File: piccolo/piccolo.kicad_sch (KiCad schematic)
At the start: 18 parts, among them U1 ProMicro

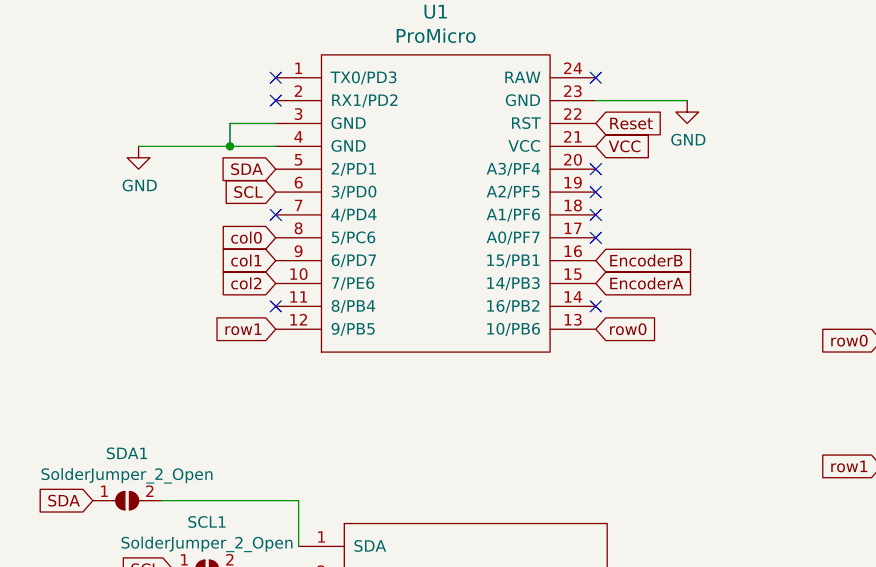
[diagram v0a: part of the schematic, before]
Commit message: flipped board, moved diodes
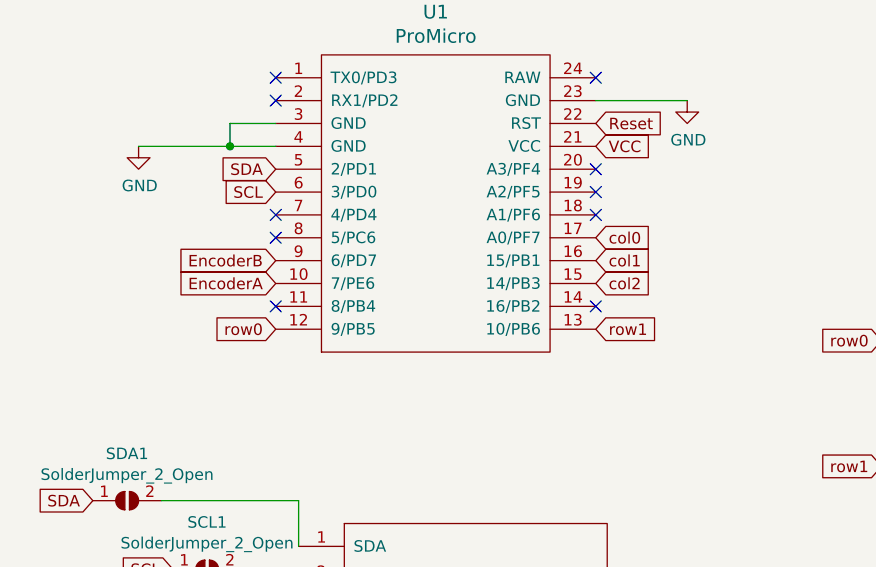
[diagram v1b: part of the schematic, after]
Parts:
- U1: footprint Envoy:ProMicro_v3 -> Envoy:ProMicro_face_in
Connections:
- net EncoderA: now also U1.10 (7/PE6); no longer U1.15 (14/PB3)
- net EncoderB: now also U1.9 (6/PD7); no longer U1.16 (15/PB1)
- net col0: now also U1.17 (A0/PF7); no longer U1.8 (5/PC6)
- net col1: now also U1.16 (15/PB1); no longer U1.9 (6/PD7)
- net col2: now also U1.15 (14/PB3); no longer U1.10 (7/PE6)
- net row0: now also U1.12 (9/PB5); no longer U1.13 (10/PB6)
- net row1: now also U1.13 (10/PB6); no longer U1.12 (9/PB5)
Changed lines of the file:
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@@
   (no_connect (at 41.91 44.45))
   (no_connect (at 41.91 57.15))
+  (no_connect (at 41.91 59.69))
   (no_connect (at 41.91 67.31))
   (no_connect (at 77.47 41.91))
@@
   (no_connect (at 77.47 54.61))
   (no_connect (at 77.47 57.15))
-  (no_connect (at 77.47 59.69))
   (no_connect (at 77.47 67.31))
   (no_connect (at 102.87 3.81))
@@
     )
   )
-  (global_label "col0" (shape input) (at 41.91 59.69 180) (fields_autoplaced)
-    (effects (font (size 1.27 1.27)) (justify right))
-    (property "Intersheet References" "${INTERSHEET_REFS}" (id 0) (at 0 0 0)
-      (effects (font (size 1.27 1.27)) hide)
-    )
-  )
-  (global_label "col1" (shape input) (at 41.91 62.23 180) (fields_autoplaced)
-    (effects (font (size 1.27 1.27)) (justify right))
-    (property "Intersheet References" "${INTERSHEET_REFS}" (id 0) (at 0 0 0)
-      (effects (font (size 1.27 1.27)) hide)
-    )
-  )
-  (global_label "col2" (shape input) (at 41.91 64.77 180) (fields_autoplaced)
-    (effects (font (size 1.27 1.27)) (justify right))
-    (property "Intersheet References" "${INTERSHEET_REFS}" (id 0) (at 0 0 0)
-      (effects (font (size 1.27 1.27)) hide)
-    )
-  )
-  (global_label "row1" (shape input) (at 41.91 69.85 180) (fields_autoplaced)
-    (effects (font (size 1.27 1.27)) (justify right))
-    (property "Intersheet References" "${INTERSHEET_REFS}" (id 0) (at 0 0 0)
+  (global_label "EncoderB" (shape input) (at 41.91 62.23 180) (fields_autoplaced)
+    (effects (font (size 1.27 1.27)) (justify right))
+    (property "Intersheet References" "${INTERSHEET_REFS}" (id 0) (at 119.38 124.46 0)
+      (effects (font (size 1.27 1.27)) hide)
+    )
+  )
+  (global_label "EncoderA" (shape input) (at 41.91 64.77 180) (fields_autoplaced)
+    (effects (font (size 1.27 1.27)) (justify right))
+    (property "Intersheet References" "${INTERSHEET_REFS}" (id 0) (at 119.38 129.54 0)
+      (effects (font (size 1.27 1.27)) hide)
+    )
+  )
+  (global_label "row0" (shape input) (at 41.91 69.85 180) (fields_autoplaced)
+    (effects (font (size 1.27 1.27)) (justify right))
+    (property "Intersheet References" "${INTERSHEET_REFS}" (id 0) (at 119.38 139.7 0)
       (effects (font (size 1.27 1.27)) hide)
     )
@@
     )
   )
-  (global_label "EncoderB" (shape input) (at 77.47 62.23 0) (fields_autoplaced)
-    (effects (font (size 1.27 1.27)) (justify left))
-    (property "Intersheet References" "${INTERSHEET_REFS}" (id 0) (at 0 0 0)
-      (effects (font (size 1.27 1.27)) hide)
-    )
-  )
-  (global_label "EncoderA" (shape input) (at 77.47 64.77 0) (fields_autoplaced)
-    (effects (font (size 1.27 1.27)) (justify left))
-    (property "Intersheet References" "${INTERSHEET_REFS}" (id 0) (at 0 0 0)
-      (effects (font (size 1.27 1.27)) hide)
-    )
-  )
-  (global_label "row0" (shape input) (at 77.47 69.85 0) (fields_autoplaced)
-    (effects (font (size 1.27 1.27)) (justify left))
-    (property "Intersheet References" "${INTERSHEET_REFS}" (id 0) (at 0 0 0)
+  (global_label "col0" (shape input) (at 77.47 59.69 0) (fields_autoplaced)
+    (effects (font (size 1.27 1.27)) (justify left))
+    (property "Intersheet References" "${INTERSHEET_REFS}" (id 0) (at 119.38 119.38 0)
+      (effects (font (size 1.27 1.27)) hide)
+    )
+  )
+  (global_label "col1" (shape input) (at 77.47 62.23 0) (fields_autoplaced)
+    (effects (font (size 1.27 1.27)) (justify left))
+    (property "Intersheet References" "${INTERSHEET_REFS}" (id 0) (at 119.38 124.46 0)
+      (effects (font (size 1.27 1.27)) hide)
+    )
+  )
+  (global_label "col2" (shape input) (at 77.47 64.77 0) (fields_autoplaced)
+    (effects (font (size 1.27 1.27)) (justify left))
+    (property "Intersheet References" "${INTERSHEET_REFS}" (id 0) (at 119.38 129.54 0)
+      (effects (font (size 1.27 1.27)) hide)
+    )
+  )
+  (global_label "row1" (shape input) (at 77.47 69.85 0) (fields_autoplaced)
+    (effects (font (size 1.27 1.27)) (justify left))
+    (property "Intersheet References" "${INTERSHEET_REFS}" (id 0) (at 119.38 139.7 0)
       (effects (font (size 1.27 1.27)) hide)
     )
@@
       (effects (font (size 1.524 1.524)))
     )
-    (property "Footprint" "Envoy:ProMicro_v3" (id 2) (at 86.36 119.38 90)
+    (property "Footprint" "Envoy:ProMicro_face_in" (id 2) (at 86.36 119.38 90)
       (effects (font (size 1.524 1.524)) hide)
     )
@@
     )
     (path "/00000000-0000-0000-0000-0000614e1eca"
-      (reference "U1") (unit 1) (value "ProMicro") (footprint "Envoy:ProMicro_v3")
+      (reference "U1") (unit 1) (value "ProMicro") (footprint "Envoy:ProMicro_face_in")
     )
     (path "/00000000-0000-0000-0000-00006157ad43"

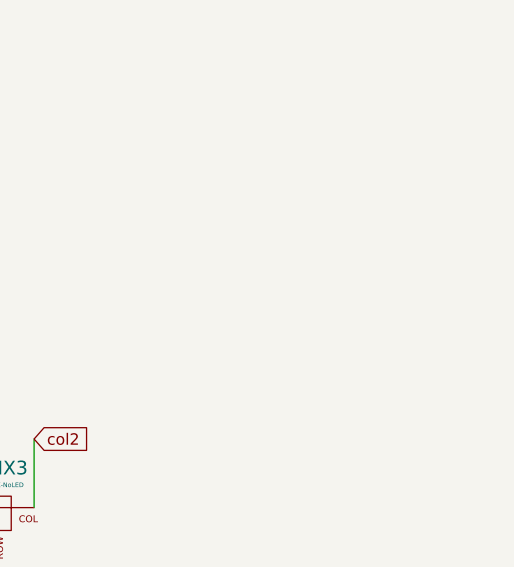
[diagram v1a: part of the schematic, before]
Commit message: Added switchplate and backplate
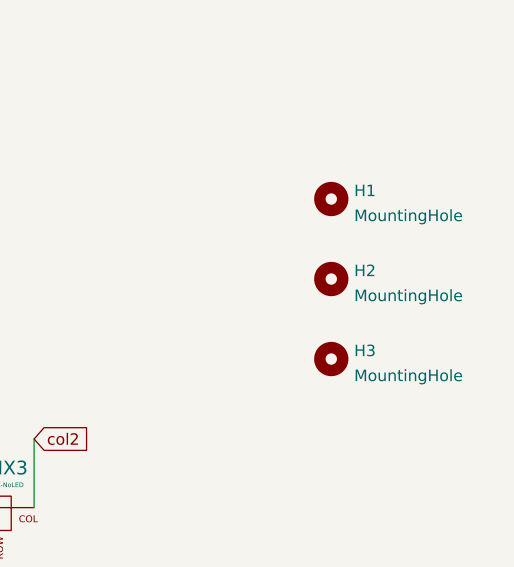
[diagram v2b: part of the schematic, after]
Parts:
- added H1, H2, H3: MountingHole, Envoy:ClearanceHole_3.7mm, symbol Mechanical:MountingHole
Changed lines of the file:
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@@
     (pin "2")
+  )
+  (symbol (lib_id "Mechanical:MountingHole") (at 180.34 30.48 0) (unit 1)
+    (in_bom yes) (on_board yes) (fields_autoplaced)
+    (property "Reference" "H1" (id 0) (at 182.8801 29.5715 0)
+      (effects (font (size 1.27 1.27)) (justify left))
+    )
+    (property "Value" "MountingHole" (id 1) (at 182.8801 32.3466 0)
+      (effects (font (size 1.27 1.27)) (justify left))
+    )
+    (property "Footprint" "Envoy:ClearanceHole_3.7mm" (id 2) (at 180.34 30.48 0)
+      (effects (font (size 1.27 1.27)) hide)
+    )
+    (property "Datasheet" "~" (id 3) (at 180.34 30.48 0)
+      (effects (font (size 1.27 1.27)) hide)
+    )
+  )
+  (symbol (lib_id "Mechanical:MountingHole") (at 180.34 39.37 0) (unit 1)
+    (in_bom yes) (on_board yes) (fields_autoplaced)
+    (property "Reference" "H2" (id 0) (at 182.8801 38.4615 0)
+      (effects (font (size 1.27 1.27)) (justify left))
+    )
+    (property "Value" "MountingHole" (id 1) (at 182.8801 41.2366 0)
+      (effects (font (size 1.27 1.27)) (justify left))
+    )
+    (property "Footprint" "Envoy:ClearanceHole_3.7mm" (id 2) (at 180.34 39.37 0)
+      (effects (font (size 1.27 1.27)) hide)
+    )
+    (property "Datasheet" "~" (id 3) (at 180.34 39.37 0)
+      (effects (font (size 1.27 1.27)) hide)
+    )
+  )
+  (symbol (lib_id "Mechanical:MountingHole") (at 180.34 48.26 0) (unit 1)
+    (in_bom yes) (on_board yes) (fields_autoplaced)
+    (property "Reference" "H3" (id 0) (at 182.8801 47.3515 0)
+      (effects (font (size 1.27 1.27)) (justify left))
+    )
+    (property "Value" "MountingHole" (id 1) (at 182.8801 50.1266 0)
+      (effects (font (size 1.27 1.27)) (justify left))
+    )
+    (property "Footprint" "Envoy:ClearanceHole_3.7mm" (id 2) (at 180.34 48.26 0)
+      (effects (font (size 1.27 1.27)) hide)
+    )
+    (property "Datasheet" "~" (id 3) (at 180.34 48.26 0)
+      (effects (font (size 1.27 1.27)) hide)
+    )
   )
   (symbol (lib_id "Jumper:SolderJumper_2_Open") (at 25.4 88.9 0) (unit 1)
@@
       (reference "GND1") (unit 1) (value "SolderJumper_2_Open") (footprint "Keyboard parts:SOLDER_JUMPER_2")
     )
+    (path "/d1639fd5-f16e-41ba-a1ac-39607ad34973"
+      (reference "H1") (unit 1) (value "MountingHole") (footprint "Envoy:ClearanceHole_3.7mm")
+    )
+    (path "/1b550bd6-2ac3-4467-8198-c0ef4abac098"
+      (reference "H2") (unit 1) (value "MountingHole") (footprint "Envoy:ClearanceHole_3.7mm")
+    )
+    (path "/9db2e03e-6cf4-4461-9b88-f24aefd4678a"
+      (reference "H3") (unit 1) (value "MountingHole") (footprint "Envoy:ClearanceHole_3.7mm")
+    )
     (path "/00000000-0000-0000-0000-0000614f0e12"

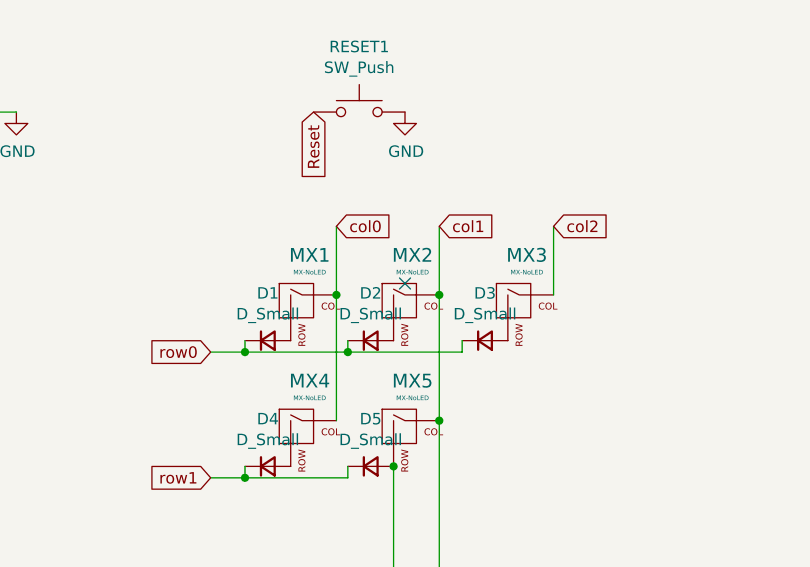
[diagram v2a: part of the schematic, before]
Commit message: Sent switchplate to PCB manufacturer for first prototype.
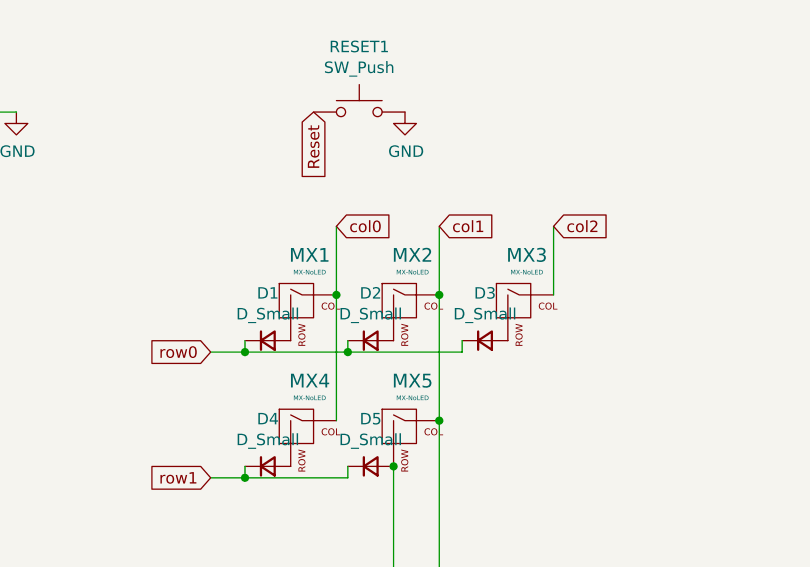
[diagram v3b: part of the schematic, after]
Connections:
- no-connect marks 12 -> 11
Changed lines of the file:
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@@
   (no_connect (at 77.47 67.31))
   (no_connect (at 102.87 3.81))
-  (no_connect (at 130.81 63.5))
   (wire (pts (xy 29.21 88.9) (xy 44.45 88.9))
     (stroke (width 0) (type default) (color 0 0 0 0))

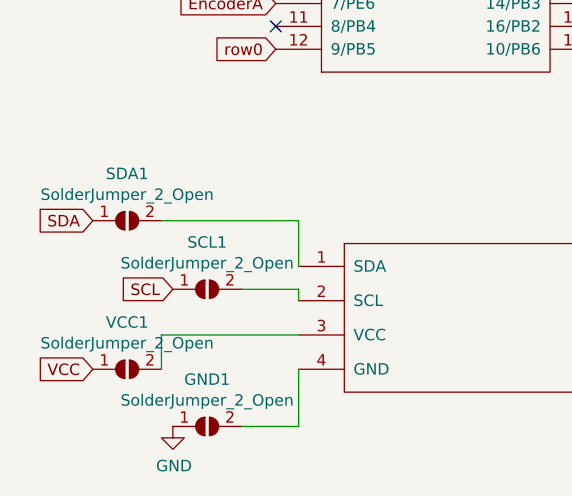
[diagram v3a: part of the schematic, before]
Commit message: make oled cutout larger in switchplate.  Prepare rev3 gerbers
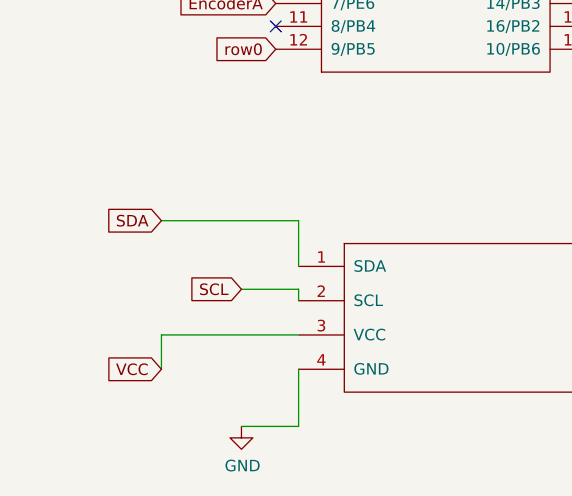
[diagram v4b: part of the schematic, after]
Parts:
- removed GND1, SCL1, SDA1, VCC1: SolderJumper_2_Open, Keyboard parts:SOLDER_JUMPER_2, symbol Jumper:SolderJumper_2_Open
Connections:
- net GND: now also OL1.4 (GND)
- net SCL: now also OL1.2 (SCL)
- net SDA: now also OL1.1 (SDA)
- net VCC: now also OL1.3 (VCC)
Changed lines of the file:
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@@
     (stroke (width 0) (type default) (color 0 0 0 0))
   )
-  (global_label "SDA" (shape input) (at 21.59 88.9 180) (fields_autoplaced)
-    (effects (font (size 1.27 1.27)) (justify right))
-    (property "Intersheet References" "${INTERSHEET_REFS}" (id 0) (at -15.24 -5.08 0)
-      (effects (font (size 1.27 1.27)) hide)
-    )
-  )
-  (global_label "VCC" (shape input) (at 21.59 105.41 180) (fields_autoplaced)
-    (effects (font (size 1.27 1.27)) (justify right))
-    (property "Intersheet References" "${INTERSHEET_REFS}" (id 0) (at -15.24 3.81 0)
-      (effects (font (size 1.27 1.27)) hide)
-    )
-  )
-  (global_label "SCL" (shape input) (at 30.48 96.52 180) (fields_autoplaced)
-    (effects (font (size 1.27 1.27)) (justify right))
-    (property "Intersheet References" "${INTERSHEET_REFS}" (id 0) (at -6.35 -1.27 0)
+  (global_label "SDA" (shape input) (at 29.21 88.9 180) (fields_autoplaced)
+    (effects (font (size 1.27 1.27)) (justify right))
+    (property "Intersheet References" "${INTERSHEET_REFS}" (id 0) (at -7.62 -5.08 0)
+      (effects (font (size 1.27 1.27)) hide)
+    )
+  )
+  (global_label "VCC" (shape input) (at 29.21 105.41 180) (fields_autoplaced)
+    (effects (font (size 1.27 1.27)) (justify right))
+    (property "Intersheet References" "${INTERSHEET_REFS}" (id 0) (at -7.62 3.81 0)
+      (effects (font (size 1.27 1.27)) hide)
+    )
+  )
+  (global_label "SCL" (shape input) (at 38.1 96.52 180) (fields_autoplaced)
+    (effects (font (size 1.27 1.27)) (justify right))
+    (property "Intersheet References" "${INTERSHEET_REFS}" (id 0) (at 1.27 -1.27 0)
       (effects (font (size 1.27 1.27)) hide)
     )
@@
     (pin "1")
   )
-  (symbol (lib_id "power:GND") (at 30.48 111.76 0) (unit 1)
-    (in_bom yes) (on_board yes)
-    (property "Reference" "#PWR0105" (id 0) (at 30.48 118.11 0)
-      (effects (font (size 1.27 1.27)) hide)
-    )
-    (property "Value" "GND" (id 1) (at 30.607 116.1542 0))
-    (property "Footprint" "" (id 2) (at 30.48 111.76 0)
-      (effects (font (size 1.27 1.27)) hide)
-    )
-    (property "Datasheet" "" (id 3) (at 30.48 111.76 0)
+  (symbol (lib_id "power:GND") (at 38.1 111.76 0) (unit 1)
+    (in_bom yes) (on_board yes)
+    (property "Reference" "#PWR0105" (id 0) (at 38.1 118.11 0)
+      (effects (font (size 1.27 1.27)) hide)
+    )
+    (property "Value" "GND" (id 1) (at 38.227 116.1542 0))
+    (property "Footprint" "" (id 2) (at 38.1 111.76 0)
+      (effects (font (size 1.27 1.27)) hide)
+    )
+    (property "Datasheet" "" (id 3) (at 38.1 111.76 0)
       (effects (font (size 1.27 1.27)) hide)
     )
@@
       (effects (font (size 1.27 1.27)) hide)
     )
-  )
-  (symbol (lib_id "Jumper:SolderJumper_2_Open") (at 25.4 88.9 0) (unit 1)
-    (in_bom no) (on_board yes)
-    (property "Reference" "SDA1" (id 0) (at 25.4 83.693 0))
-    (property "Value" "SolderJumper_2_Open" (id 1) (at 25.4 86.0044 0))
-    (property "Footprint" "Keyboard parts:SOLDER_JUMPER_2" (id 2) (at 25.4 88.9 0)
-      (effects (font (size 1.27 1.27)) hide)
-    )
-    (property "Datasheet" "~" (id 3) (at 25.4 88.9 0)
-      (effects (font (size 1.27 1.27)) hide)
-    )
-    (pin "1")
-    (pin "2")
-  )
-  (symbol (lib_id "Jumper:SolderJumper_2_Open") (at 25.4 105.41 0) (unit 1)
-    (in_bom no) (on_board yes)
-    (property "Reference" "VCC1" (id 0) (at 25.4 100.203 0))
-    (property "Value" "SolderJumper_2_Open" (id 1) (at 25.4 102.5144 0))
-    (property "Footprint" "Keyboard parts:SOLDER_JUMPER_2" (id 2) (at 25.4 105.41 0)
-      (effects (font (size 1.27 1.27)) hide)
-    )
-    (property "Datasheet" "~" (id 3) (at 25.4 105.41 0)
-      (effects (font (size 1.27 1.27)) hide)
-    )
-    (pin "1")
-    (pin "2")
-  )
-  (symbol (lib_id "Jumper:SolderJumper_2_Open") (at 34.29 96.52 0) (unit 1)
-    (in_bom no) (on_board yes)
-    (property "Reference" "SCL1" (id 0) (at 34.29 91.313 0))
-    (property "Value" "SolderJumper_2_Open" (id 1) (at 34.29 93.6244 0))
-    (property "Footprint" "Keyboard parts:SOLDER_JUMPER_2" (id 2) (at 34.29 96.52 0)
-      (effects (font (size 1.27 1.27)) hide)
-    )
-    (property "Datasheet" "~" (id 3) (at 34.29 96.52 0)
-      (effects (font (size 1.27 1.27)) hide)
-    )
-    (pin "1")
-    (pin "2")
-  )
-  (symbol (lib_id "Jumper:SolderJumper_2_Open") (at 34.29 111.76 0) (unit 1)
-    (in_bom no) (on_board yes)
-    (property "Reference" "GND1" (id 0) (at 34.29 106.553 0))
-    (property "Value" "SolderJumper_2_Open" (id 1) (at 34.29 108.8644 0))
-    (property "Footprint" "Keyboard parts:SOLDER_JUMPER_2" (id 2) (at 34.29 111.76 0)
-      (effects (font (size 1.27 1.27)) hide)
-    )
-    (property "Datasheet" "~" (id 3) (at 34.29 111.76 0)
-      (effects (font (size 1.27 1.27)) hide)
-    )
-    (pin "1")
-    (pin "2")
   )
   (symbol (lib_id "Switch:SW_Push") (at 125.73 44.45 0) (unit 1)
@@
       (reference "ENC1") (unit 1) (value "Rotary_Encoder_Switch") (footprint "Keebio-Parts:RotaryEncoder_EC11-no-legs")
     )
-    (path "/00000000-0000-0000-0000-00006157b160"
-      (reference "GND1") (unit 1) (value "SolderJumper_2_Open") (footprint "Keyboard parts:SOLDER_JUMPER_2")
-    )
     (path "/d1639fd5-f16e-41ba-a1ac-39607ad34973"
       (reference "H1") (unit 1) (value "MountingHole") (footprint "Envoy:ClearanceHole_3.7mm")
@@
       (reference "RESET1") (unit 1) (value "SW_Push") (footprint "Envoy:Reset_Jumper_Points")
     )
-    (path "/00000000-0000-0000-0000-00006157a6d9"
-      (reference "SCL1") (unit 1) (value "SolderJumper_2_Open") (footprint "Keyboard parts:SOLDER_JUMPER_2")
-    )
-    (path "/00000000-0000-0000-0000-000061578c34"
-      (reference "SDA1") (unit 1) (value "SolderJumper_2_Open") (footprint "Keyboard parts:SOLDER_JUMPER_2")
-    )
     (path "/00000000-0000-0000-0000-0000614e1eca"
       (reference "U1") (unit 1) (value "ProMicro") (footprint "Envoy:ProMicro_face_in")
     )
-    (path "/00000000-0000-0000-0000-00006157ad43"
-      (reference "VCC1") (unit 1) (value "SolderJumper_2_Open") (footprint "Keyboard parts:SOLDER_JUMPER_2")
-    )
-  )
+  )
